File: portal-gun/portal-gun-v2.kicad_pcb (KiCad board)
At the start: 2 copper layers, 107.2 x 55.5 mm, 17 parts, among them J1 SAO

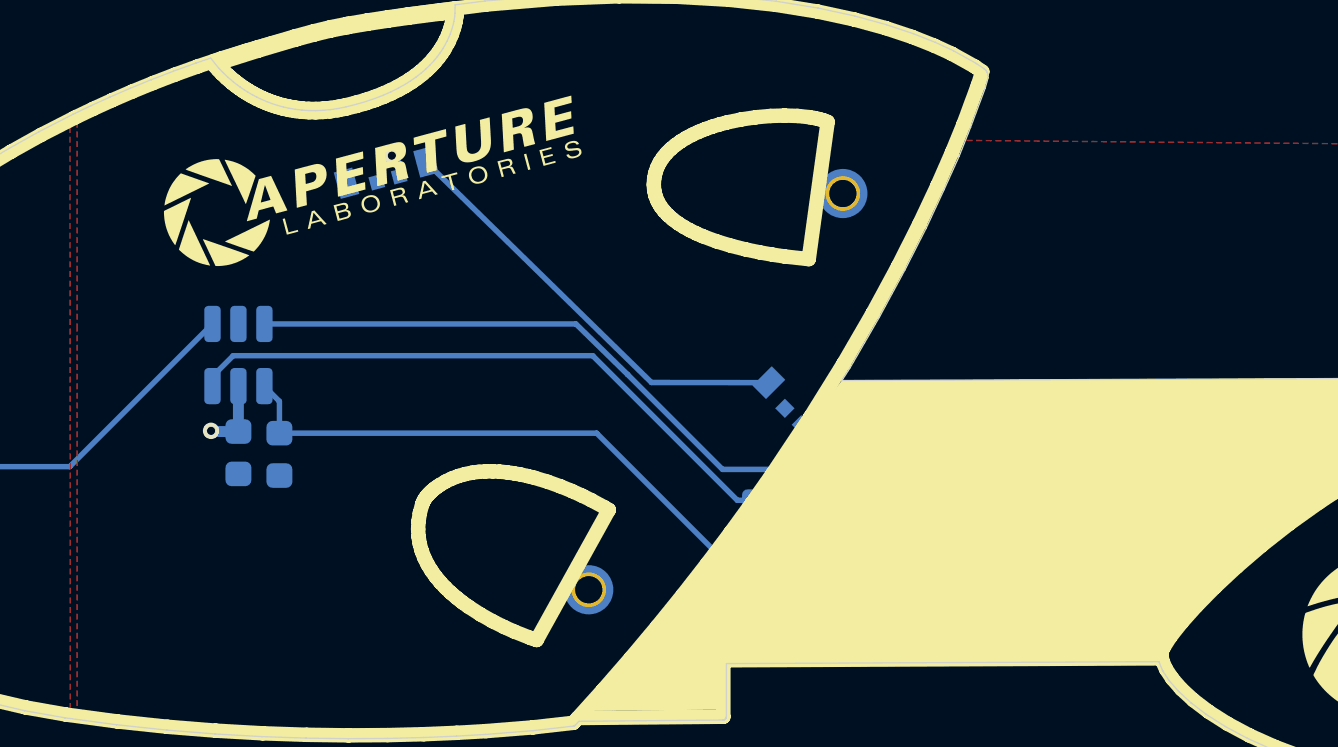
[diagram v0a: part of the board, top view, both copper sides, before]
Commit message: added res to pin 6 for output
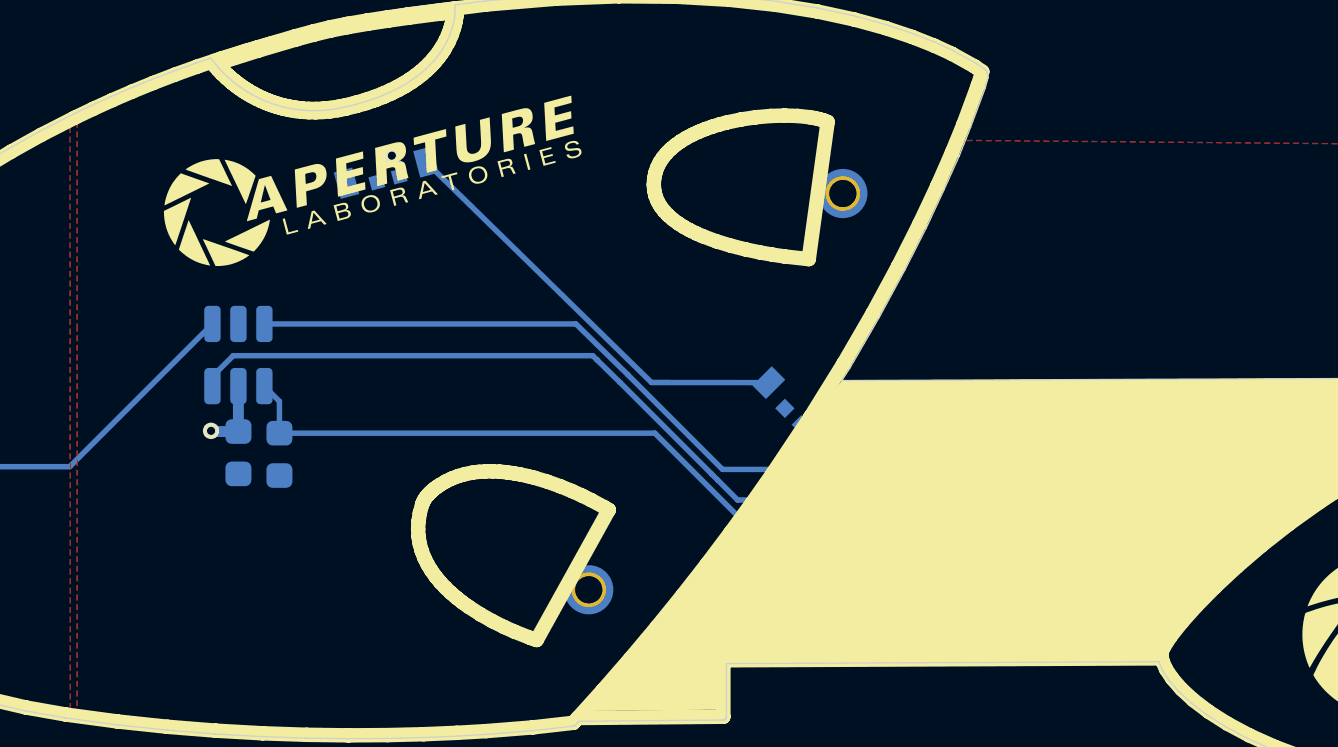
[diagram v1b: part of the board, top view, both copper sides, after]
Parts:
- removed R1: R_Small, Resistor_SMD:R_0603_1608Metric
- J1: footprint Connector_PinHeader_2.54mm:PinHeader_2x03_P2.54mm_Vertical -> Connector_PinSocket_2.54mm:IDC-TH_6P-P2.54_DS1013-06SSIB1-B-0
- moved J1 2.84 mm to (155.3, 86.7), turned to 0 degrees
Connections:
- J1 pad 6: Net-(J1-Pin_6) -> unconnected-(J1-Pin_6-Pad6)
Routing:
- net Net-(J1-Pin_6): track 15.5 -> 0.00 mm
